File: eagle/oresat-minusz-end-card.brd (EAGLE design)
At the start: 99 x 95.3 mm, 17 parts, among them J1 J-SAMTEC-TFM-110-X1-XXX-D-RA, J2 U.FL, J3 U.FL, J4 U.FL

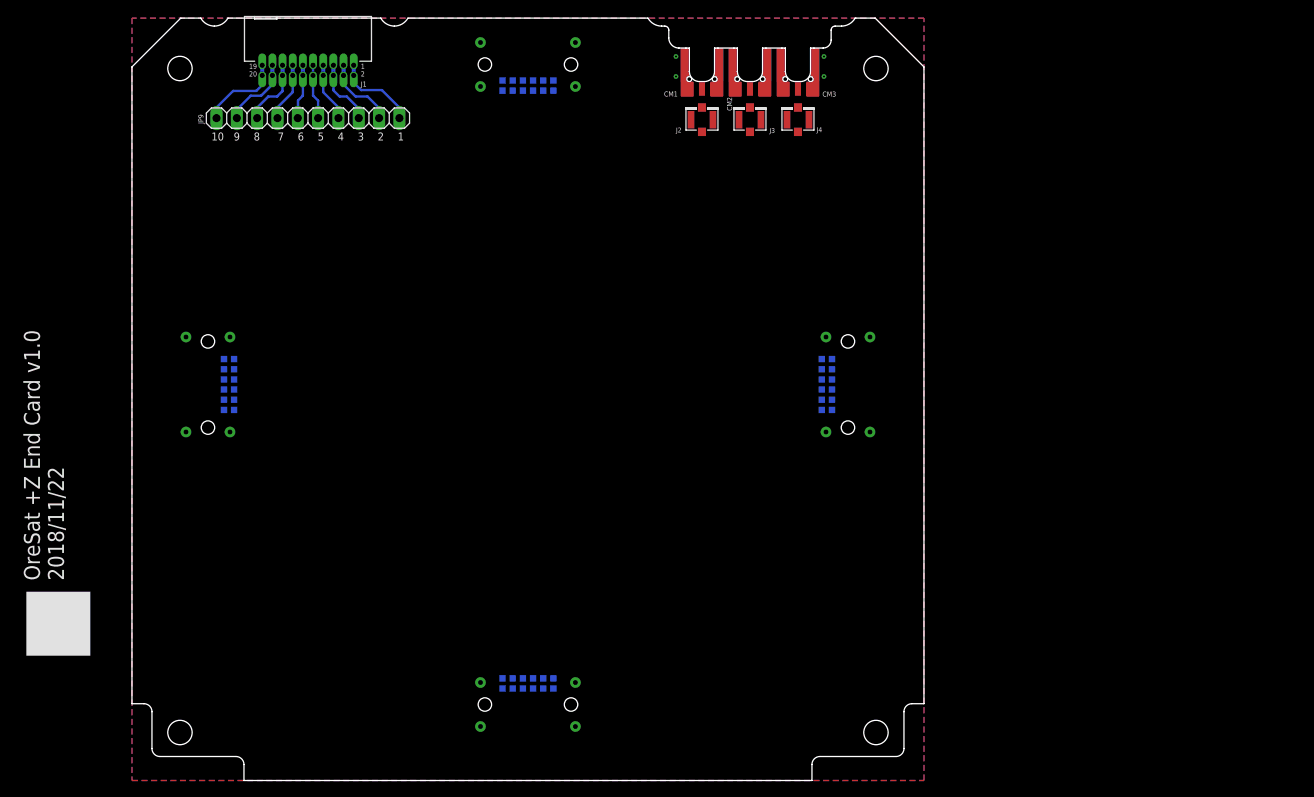
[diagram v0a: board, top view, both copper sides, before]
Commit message: Updated end cards with antenna keep outs, and rewired +Z end card debug port and started on +Z schematic update with power domain.
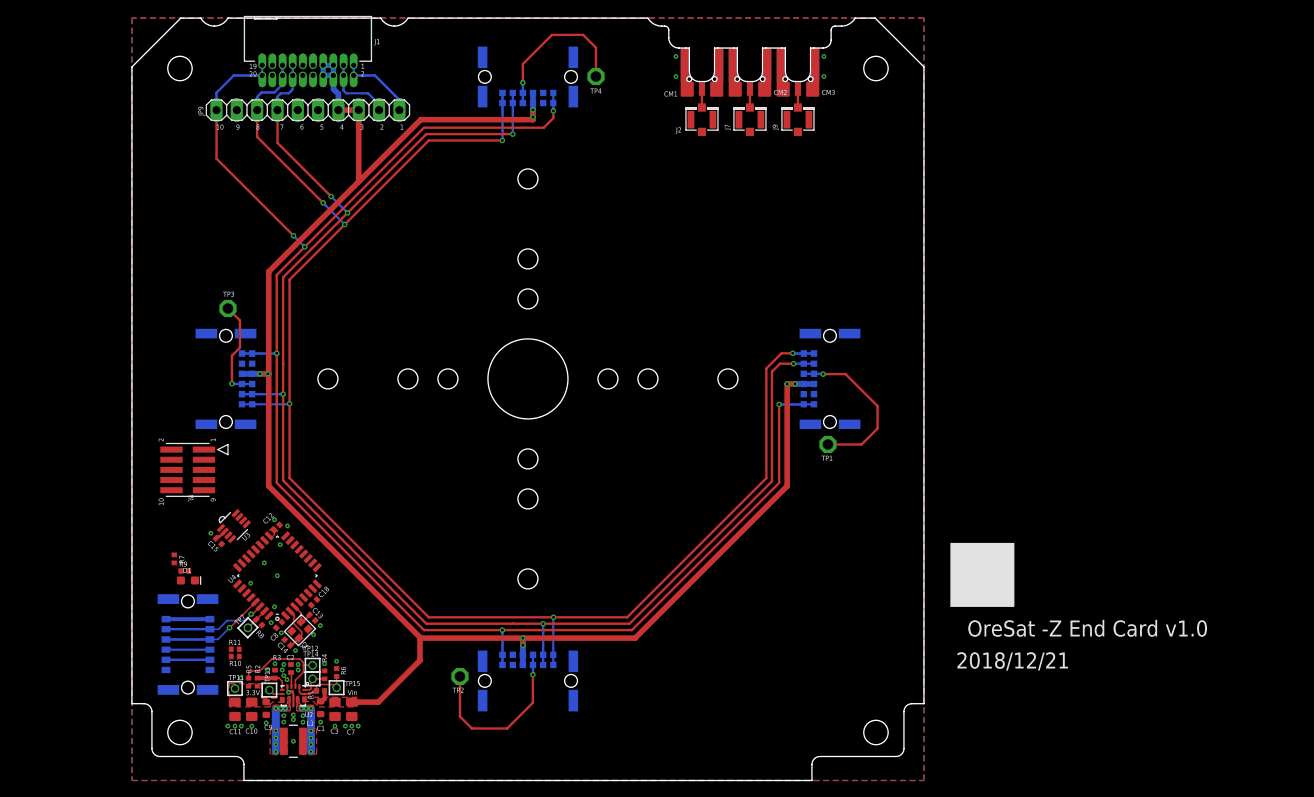
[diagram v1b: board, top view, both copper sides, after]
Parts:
- removed CM4, CM5, CM6, CM7: ORESAT-SOLARPANEL-CARD-12PIN, oresat-connectors:CON-1.27-M-RA-HARTING-1515012X401XXX
- added C1: 10u, oresat-rcl:.0603-B-NOSILK
- added C10, C11: 22u, oresat-rcl:.0805-B-NOSILK
- added C12, C15, C18, C2, C8: 100n, rcl_custom:.0402-B-NOSILK
- added C13, C14: 20p, rcl_custom:.0402-B-NOSILK
- added C3, C7: 10u, oresat-rcl:.0805-B-NOSILK
- added C9: 22u, oresat-rcl:.0603-B-NOSILK
- added CF1: M55-7011242R, J-Harwin-M55-6021242R:HARWIN-M55-6021242R
- added D1: GREEN, SparkFun-LED:LED-0603
- added J5, J6: M55-7101242R, J-Harwin-M55-7101242:M55-7101242R
- added J7, J9: U.FL, SparkFun-Connectors:U.FL
- added J8: FTSH-105-XX-X-DV-K, J-Samtec-FTSH-105-XXX-DV-K-ARM-SWD:CON10_2X5_DUK_FTSH
- added L1: 1.5 uH, L-Coilcraft-XFL4020:L-COILCRAFT-XFL4020
- added R1, R11, R4, R8: 10k, rcl_custom:.0402-B-NOSILK
- added R10, R7: 4.7k, rcl_custom:.0402-B-NOSILK
- added R2: 470k, rcl_custom:.0402-B-NOSILK
- added R3: 150k, rcl_custom:.0402-B-NOSILK
- added R5, R6: NP, rcl_custom:.0402-B-NOSILK
- added R9: 2.7k, rcl_custom:.0402-B-NOSILK
- added TP1, TP2, TP3, TP4: TPPAD1-13, testpad:P1-13
- added TP11, TP12, TP13, TP14, TP15, TP7: TEST-POINT, Tova:2MM-TEST-POINT
- added U2: TPS63070, ic-pwr-tps63070x:TPS63070X
- added U3: TCAN330, TCAN330:SOT23-8_TI-DCN
- added U4: STM32F042K6, STM32F042K:QFP32-7X7
- added X2: 16MHZ-2.5x2mm, low-gain-radio:CRYSTAL_2.5X2
- J3, J4: value U.FL -> M55-7101242R; device SparkFun-Connectors:U.FL -> J-Harwin-M55-7101242:M55-7101242R
- moved J4 77.8 mm to (49.5, 12.4), flipped to the bottom, turned to 0 degrees
- moved J3 33.9 mm to (87.2, 50.2), flipped to the bottom, turned to 270 degrees
- moved JP9 1.00 mm to (22.0, 83.8)
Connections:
- net AUX_CAN2_H renamed CAN2_H
- net AUX_CAN2_L renamed CAN2_L
- removed net AUX_!SHUTDOWN: J1.19, J1.20, JP9.10
- removed net AUX_CAN1_H: J1.13, J1.14, JP9.7
- removed net AUX_CAN1_L: J1.15, J1.16, JP9.8
- removed net AUX_GND1: J1.17, J1.18, JP9.9
- removed net AUX_GND2: J1.11, J1.12, JP9.6
- removed net AUX_GND3: J1.10, J1.9, JP9.5
- removed net AUX_VBUS1: J1.7, J1.8, JP9.4
- removed net AUX_VBUS2: J1.5, J1.6, JP9.3
- removed net N$300: CM3.RF, J4.FEED
- new net !SHUTDOWN: J1.19, J1.20, J3.1, J3.2, J4.1, J4.2, J5.1, J5.2, J6.1, J6.2, JP9.10
- new net 3.3V: C10.1, C11.1, C12.2, C15.2, C18.2, C8.2, C9.1, CF1.11, CF1.12, J8.1, R10.2, R11.2, R2.2, R5.2, R7.2, TP11.1, U2.7-8, U3.3, U4.1, U4.17, U4.5
- new net BOOT1: R8.2, TP7.1, U4.31
- new net CAN1_H: J1.13, J1.14, J3.10, J3.9, J4.10, J4.9, J5.10, J5.9, J6.10, J6.9, JP9.7, U3.7
- new net CAN1_L: J1.15, J1.16, J3.11, J3.12, J4.11, J4.12, J5.11, J5.12, J6.11, J6.12, JP9.8, U3.6
- new net CAN_RX: U3.4, U4.21
- new net CAN_SHDN: U3.5, U4.20
- new net CAN_SILENT: U3.8, U4.19
- new net CAN_TX: U3.1, U4.22
- new net CRYSTALIN1: C14.1, U4.2, X2.1
- new net CRYSTALOUT1: C13.1, U4.3, X2.3
- new net N$1: J4.7, J4.8, TP2.TP
- new net N$2: J3.7, J3.8, TP1.TP
- new net N$4: J5.7, J5.8, TP3.TP
- new net N$5: J6.7, J6.8, TP4.TP
- new net N$7: D1.A, R9.1
- new net NRESET: J8.10, U4.4
- new net PA0: R9.2, U4.6
- new net PA1: U4.7
- new net PA15: U4.25
- new net PA2/USART2_TX: U4.8
- new net PA3/USART2_RX: U4.9
- new net PA4: U4.10
- new net PA5/SPI1_SCK: U4.11
- new net PA6/SPI1_MISO: U4.12
- new net PA7/SPI1_MOSI: U4.13
- new net PA8: U4.18
- new net PB0: U4.14
- new net PB1: U4.15
- new net PB3: U4.26
- new net PB4/I2C-!RESET: CF1.3, CF1.4, U4.27
- new net PB5/I2C-!INT: CF1.5, CF1.6, R11.1, U4.28
- new net PB6/SCL: CF1.7, CF1.8, R7.1, U4.29
- new net PB7/SDA: CF1.10, CF1.9, R10.1, U4.30
- new net RF3: CM3.RF, J9.FEED
- new net SWCLK: J8.4, U4.24
- new net SWDIO: J8.2, U4.23
- new net TPS-EN2: R1.1, R6.2, TP15.1, U2.1, U2.14
- new net TPS-FB2: R2.1, R3.2, U2.5
- new net TPS-FB4: TP13.1, U2.6
- new net TPS-L1: L1.1, U2.11
- new net TPS-L2: L1.2, U2.9
- new net TPS-PG2: R5.1, TP12.1, U2.2
- new net TPS-VAUX2: C2.1, U2.3
- new net TPS-VSEL2: R4.2, TP14.1, U2.15
- new net VBUS: C1.1, C3.1, C7.1, J1.5, J1.6, J1.7, J1.8, J3.5, J3.6, J4.5, J4.6, J5.5, J5.6, J6.5, J6.6, JP9.3, JP9.4, R1.2, U2.12-13
- net GND: now also C1.2, C10.2, C11.2, C12.1, C13.2, C14.2, C15.1, C18.1, C2.2, C3.2, C7.2, C8.1, C9.2, CF1.1, CF1.2, CF1.P$1, CF1.P$2, CF1.P$3, CF1.P$4, D1.C, J1.10, J1.11, J1.12, J1.17, J1.18, J1.9, J3.3, J3.4, J3.P$1, J3.P$2, J3.P$3, J3.P$4, J4.3, J4.4, J4.P$1, J4.P$2, J4.P$3, J4.P$4, J5.3, J5.4, J5.P$1, J5.P$2, J5.P$3, J5.P$4, J6.3, J6.4, J6.P$1, J6.P$2, J6.P$3, J6.P$4, J7.1, J7.2, J8.3, J8.5, J8.9, J9.1, J9.2, JP9.5, JP9.6, JP9.9, R3.1, R4.1, R6.1, R8.1, U2.10, U2.4, U3.2, U4.16, U4.32, X2.2, X2.4; no longer J3.1, J3.2, J4.1, J4.2
- net RF2: now also J7.FEED; no longer J3.FEED
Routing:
- net VBUS: track 0.00 -> 214.6 mm, vias 0 -> 8
- net !SHUTDOWN: track 0.00 -> 204.5 mm, vias 0 -> 6
- net CAN1_L: track 0.00 -> 197.7 mm, vias 0 -> 6
- net CAN1_H: track 0.00 -> 195.7 mm, vias 0 -> 6
- net N$1: track 0.00 -> 22.1 mm, vias 0 -> 1
- net N$2: track 0.00 -> 20.7 mm, vias 0 -> 1
- net N$5: track 0.00 -> 19.8 mm, vias 0 -> 1
- net PB6/SCL: track 0.00 -> 13.1 mm, vias 0 -> 1
- net N$4: track 0.00 -> 13.0 mm, vias 0 -> 1
- net PB7/SDA: track 0.00 -> 12.9 mm, vias 0 -> 1
- net TPS-PG2: track 0.00 -> 12.9 mm
- net AUX_!SHUTDOWN: track 10.7 -> 0.00 mm
- net AUX_GND1: track 9.21 -> 0.00 mm
- net AUX_CAN1_L: track 8.56 -> 0.00 mm
- net AUX_VBUS2: track 8.45 -> 0.00 mm
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- added copper zone on layer 1, net 3.3V
- added copper zone on layer 1, net TPS-L1
- added copper zone on layer 1, net TPS-L2
- added copper zone on layer 1, net VBUS
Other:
- board text added: "2018/12/21"
- board text added: "3.3V"
- board text added: "OreSat -Z End Card v1.0"
- board text added: "Vin"
- board text removed: "2018/11/22"
- board text removed: "OreSat +Z End Card v1.0"
